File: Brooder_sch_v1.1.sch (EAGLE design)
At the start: 25 parts, among them J1 DCJ0202, J2 1X2-3.5MM, U1 328P

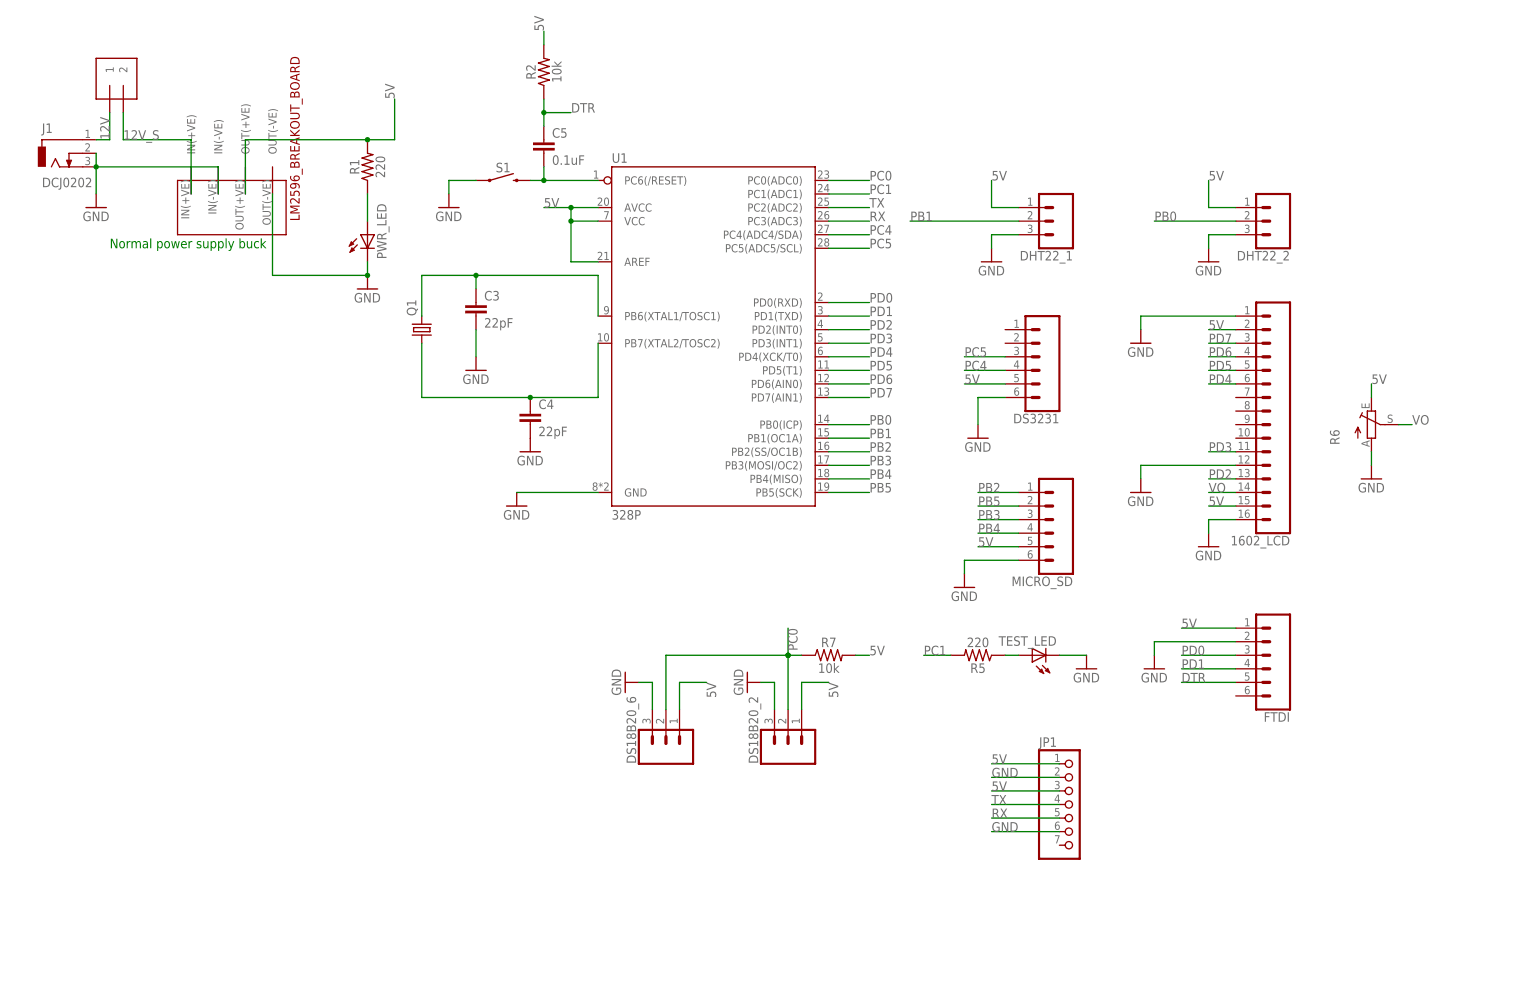
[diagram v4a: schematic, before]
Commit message: Adds separate power source for sim800l and board
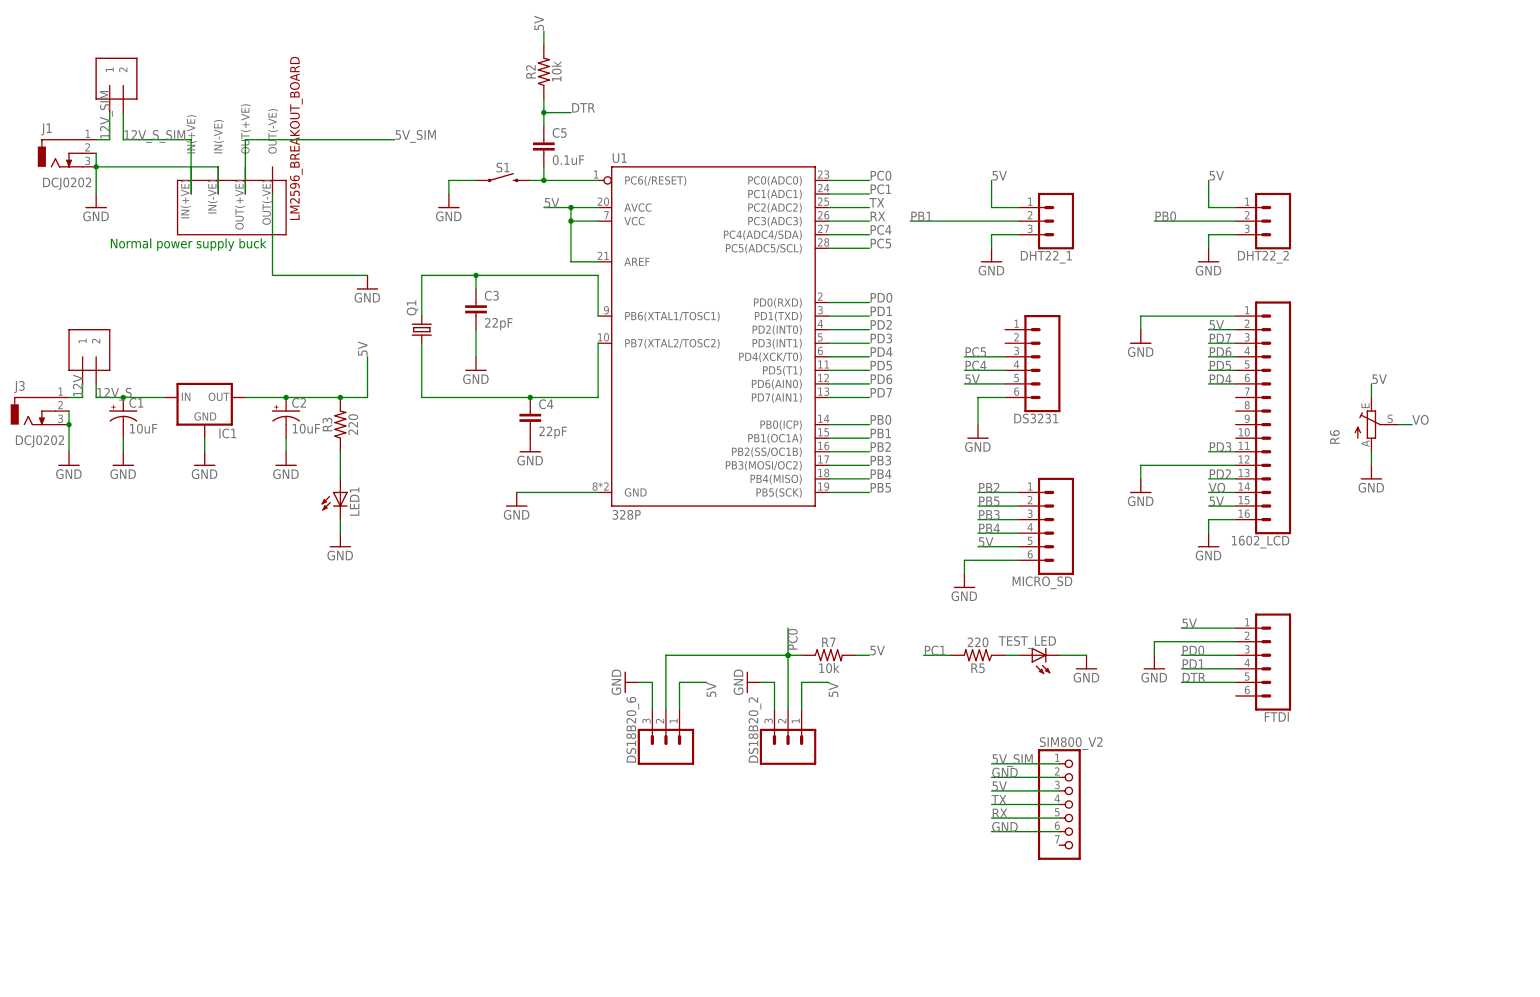
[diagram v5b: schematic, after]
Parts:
- removed PWR_LED: (no value), adafruit:LED5MM
- removed R1: 220, SparkFun-Resistors:10MOHM-HORIZ-1/4W-5%
- added C1, C2: 10uF, SparkFun-Capacitors:10UF-POLAR-RADIAL-2.5MM-25V-20%
- added IC1: (no value), v-reg:78XXS
- added J3: DCJ0202, con-jack:DCJ0202
- added J4: 1X2-3.5MM, adafruit:1X2-3.5MM
- added LED1: (no value), adafruit:LED5MM
- added R3: 220, SparkFun-Resistors:10MOHM-HORIZ-1/4W-5%
- renumbered JP1 to SIM800_V2
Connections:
- removed net N$3: PWR_LED.A, R1.1
- new net 12V_SIM: J1.1, J2.1
- new net 12V_S_SIM: J2.2, U$2.IN(+VE)
- new net 5V_SIM: SIM800_V2.1, U$2.OUT(+VE)
- new net N$2: LED1.A, R3.1
- net 12V: now also J3.1, J4.1; no longer J1.1, J2.1
- net 12V_S: now also C1.+, IC1.IN, J4.2; no longer J2.2, U$2.IN(+VE)
- net 5V: now also C2.+, IC1.OUT, R3.2; no longer R1.2, SIM800_V2.1, U$2.OUT(+VE)
- net GND: now also C1.-, C2.-, IC1.GND, J3.2, J3.3, LED1.C; no longer PWR_LED.C

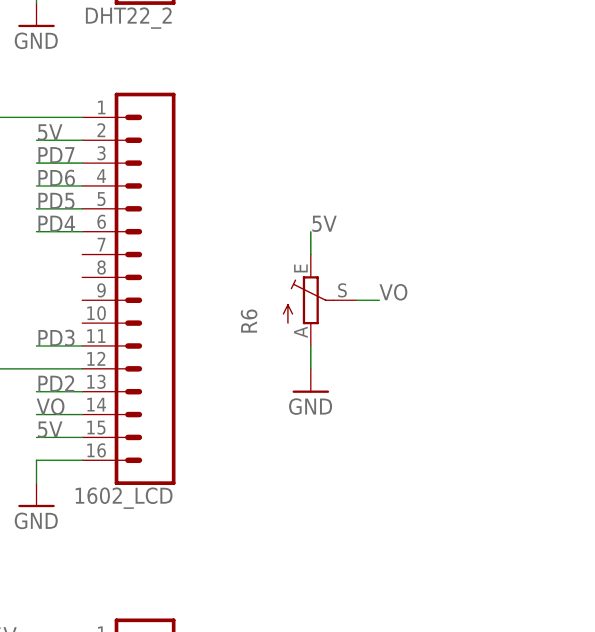
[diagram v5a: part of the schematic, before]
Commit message: Replaces pot rj6 with pot ct6
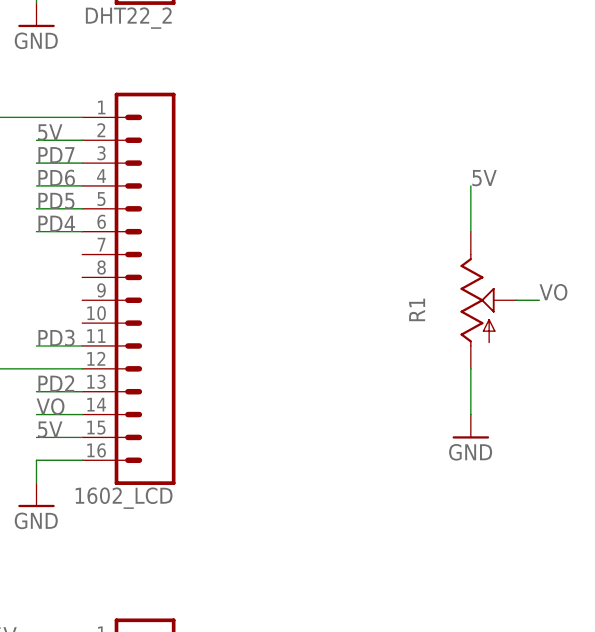
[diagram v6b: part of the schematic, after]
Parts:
- removed R6: (no value), pot:TRIM_EU-RJ6
- added R1: (no value), pot:TRIM_US-CT6
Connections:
- net 5V: now also R1.E; no longer R6.E
- net GND: now also R1.A; no longer R6.A
- net VO: now also R1.S; no longer R6.S
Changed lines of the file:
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@@
 <part name="TEST_LED" library="adafruit" deviceset="LED" device="5MM"/>
 <part name="GND16" library="supply1" library_urn="urn:adsk.eagle:library:371" deviceset="GND" device=""/>
-<part name="R6" library="pot" library_urn="urn:adsk.eagle:library:331" deviceset="TRIM_EU-" device="RJ6" package3d_urn="urn:adsk.eagle:package:22699/1"/>
-<part name="GND24" library="supply1" library_urn="urn:adsk.eagle:library:371" deviceset="GND" device=""/>
 <part name="DS3231" library="SparkFun-Connectors" deviceset="CONN_06" device="NO_SILK_FEMALE_PTH"/>
 <part name="GND25" library="supply1" library_urn="urn:adsk.eagle:library:371" deviceset="GND" device=""/>
@@
 <part name="GND20" library="supply1" library_urn="urn:adsk.eagle:library:371" deviceset="GND" device=""/>
 <part name="J4" library="adafruit" deviceset="1X2" device="-3.5MM"/>
+<part name="R1" library="pot" library_urn="urn:adsk.eagle:library:331" deviceset="TRIM_US-" device="CT6" package3d_urn="urn:adsk.eagle:package:22692/1"/>
+<part name="GND21" library="supply1" library_urn="urn:adsk.eagle:library:371" deviceset="GND" device=""/>
 </parts>
 <sheets>
@@
 <attribute name="VALUE" x="121.92" y="10.16" size="1.778" layer="96"/>
 </instance>
-<instance part="R6" gate="1" x="177.8" y="58.42"/>
-<instance part="GND24" gate="1" x="177.8" y="48.26" smashed="yes">
-<attribute name="VALUE" x="175.26" y="45.72" size="1.778" layer="96"/>
-</instance>
 <instance part="DS3231" gate="G$1" x="114.3" y="71.12" smashed="yes" rot="R180">
 <attribute name="VALUE" x="119.38" y="81.026" size="1.778" layer="96" font="vector" rot="R180"/>
@@
 </instance>
 <instance part="J4" gate="G$1" x="-60.96" y="71.12" rot="R90"/>
+<instance part="R1" gate="G$1" x="195.58" y="58.42"/>
+<instance part="GND21" gate="1" x="195.58" y="43.18" smashed="yes">
+<attribute name="VALUE" x="193.04" y="40.64" size="1.778" layer="96"/>
+</instance>
 </instances>
 <busses>
@@
 </segment>
 <segment>
-<pinref part="R6" gate="1" pin="A"/>
-<wire x1="177.8" y1="53.34" x2="177.8" y2="50.8" width="0.1524" layer="91"/>
-<pinref part="GND24" gate="1" pin="GND"/>
-</segment>
-<segment>
 <pinref part="DS3231" gate="G$1" pin="6"/>
 <wire x1="109.22" y1="63.5" x2="104.14" y2="63.5" width="0.1524" layer="91"/>
@@
 <pinref part="GND20" gate="1" pin="GND"/>
 <wire x1="-15.24" y1="40.64" x2="-15.24" y2="38.1" width="0.1524" layer="91"/>
+</segment>
+<segment>
+<pinref part="R1" gate="G$1" pin="A"/>
+<wire x1="195.58" y1="50.8" x2="195.58" y2="45.72" width="0.1524" layer="91"/>
+<pinref part="GND21" gate="1" pin="GND"/>
 </segment>
 </net>
@@
 </segment>
 <segment>
-<pinref part="R6" gate="1" pin="E"/>
-<wire x1="177.8" y1="63.5" x2="177.8" y2="66.04" width="0.1524" layer="91"/>
-<label x="177.8" y="66.04" size="1.778" layer="95"/>
-</segment>
-<segment>
 <pinref part="DS3231" gate="G$1" pin="5"/>
 <wire x1="109.22" y1="66.04" x2="101.6" y2="66.04" width="0.1524" layer="91"/>
@@
 <label x="-10.16" y="71.12" size="1.778" layer="95" rot="R90"/>
 </segment>
+<segment>
+<pinref part="R1" gate="G$1" pin="E"/>
+<wire x1="195.58" y1="66.04" x2="195.58" y2="71.12" width="0.1524" layer="91"/>
+<label x="195.58" y="71.12" size="1.778" layer="95"/>
+</segment>
 </net>
 <net name="N$4" class="0">
@@
 </segment>
 <segment>
-<pinref part="R6" gate="1" pin="S"/>
-<wire x1="182.88" y1="58.42" x2="185.42" y2="58.42" width="0.1524" layer="91"/>
-<label x="185.42" y="58.42" size="1.778" layer="95"/>
-</segment>
-</net>
+<pinref part="R1" gate="G$1" pin="S"/>
+<wire x1="200.66" y1="58.42" x2="203.2" y2="58.42" width="0.1524" layer="91"/>
+<label x="203.2" y="58.42" size="1.778" layer="95"/>
+</segment>
+</net>
